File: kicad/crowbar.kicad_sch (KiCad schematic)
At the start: 7 parts

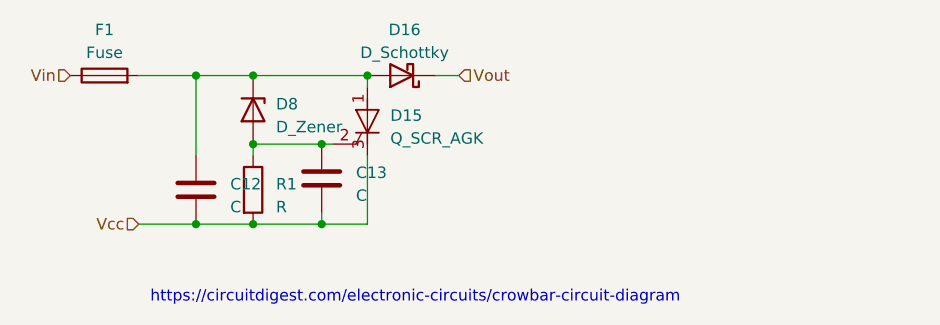
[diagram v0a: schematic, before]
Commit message: Subdivide circuits into hierarchical sheets
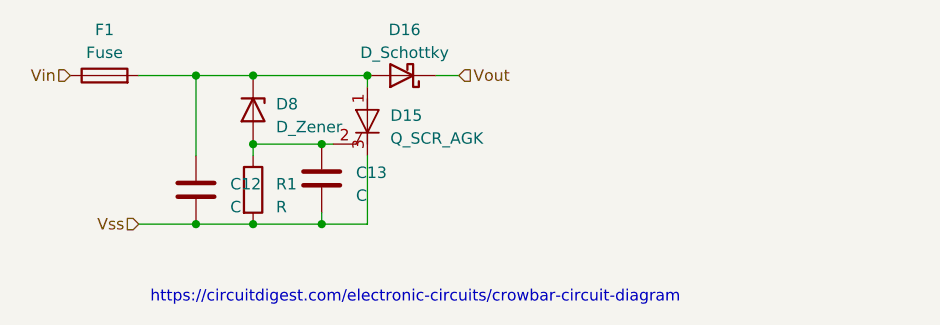
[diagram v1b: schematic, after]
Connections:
- net Vcc renamed Vss
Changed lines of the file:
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@@
     (effects (font (size 1.27 1.27)) (justify right))
   )
-  (hierarchical_label "Vcc" (shape input) (at 74.93 93.98 180) (fields_autoplaced)
+  (hierarchical_label "Vss" (shape input) (at 74.93 93.98 180) (fields_autoplaced)
     (effects (font (size 1.27 1.27)) (justify right))
   )
